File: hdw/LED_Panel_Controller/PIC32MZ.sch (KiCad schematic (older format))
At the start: 3 parts, among them U1101 PIC32MZ2048EFG100_IPF

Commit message: having a mid-project crisis
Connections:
- net WIFI_CHIP_EN: no longer names the net of U1101.79 (RD12/EBID12/ETXD2/RPD12/PMD12)
- net WIFI_Stream_Mode_LED renamed MLVDS_Stream_Mode_LED
- net WIFI_WAKE: no longer names the net of U1101.82 (RD5/~SQICS1~/RPD5)
- net ~WIFI_IRQN: no longer names the net of U1101.47 (RD14/AN32/AETXD0/RPD14)
- net ~WIFI_RESET: no longer names the net of U1101.81 (RD4/~SQICS0~/RPD4)
- net ~WIFI_SPI_SS: no longer names the net of U1101.80 (RD13/EBID13/ETXD3/PMD13)
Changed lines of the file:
@@
 Text GLabel 3020 5000 0    50   Input ~ 0
 PIC32MZ_SOSC_EC
-Text GLabel 7020 1700 2    40   Output ~ 0
-~WIFI_RESET
-Text GLabel 7020 1800 2    50   Output ~ 0
-WIFI_WAKE
-Text GLabel 7020 2200 2    50   Output ~ 0
-WIFI_CHIP_EN
 Text GLabel 7020 2000 2    50   Output ~ 0
 WIFI_SPI_SCK
-Text GLabel 7020 2300 2    40   Output ~ 0
-~WIFI_SPI_SS
 Text GLabel 7020 2100 2    50   Output ~ 0
 WIFI_SPI_MOSI
 Text GLabel 7020 2500 2    50   Input ~ 0
 WIFI_SPI_MISO
-Text GLabel 7020 2400 2    40   Input ~ 0
-~WIFI_IRQN
 $Comp
 L Custom_Library:GNDA_MZ #PWR01103
@@
 ~FLASH_SPI_CE7
 Text GLabel 3020 3450 0    50   Output ~ 0
-WIFI_Stream_Mode_LED
+MLVDS_Stream_Mode_LED
 Text Notes 9720 1950 0    50   ~ 0
 OC5

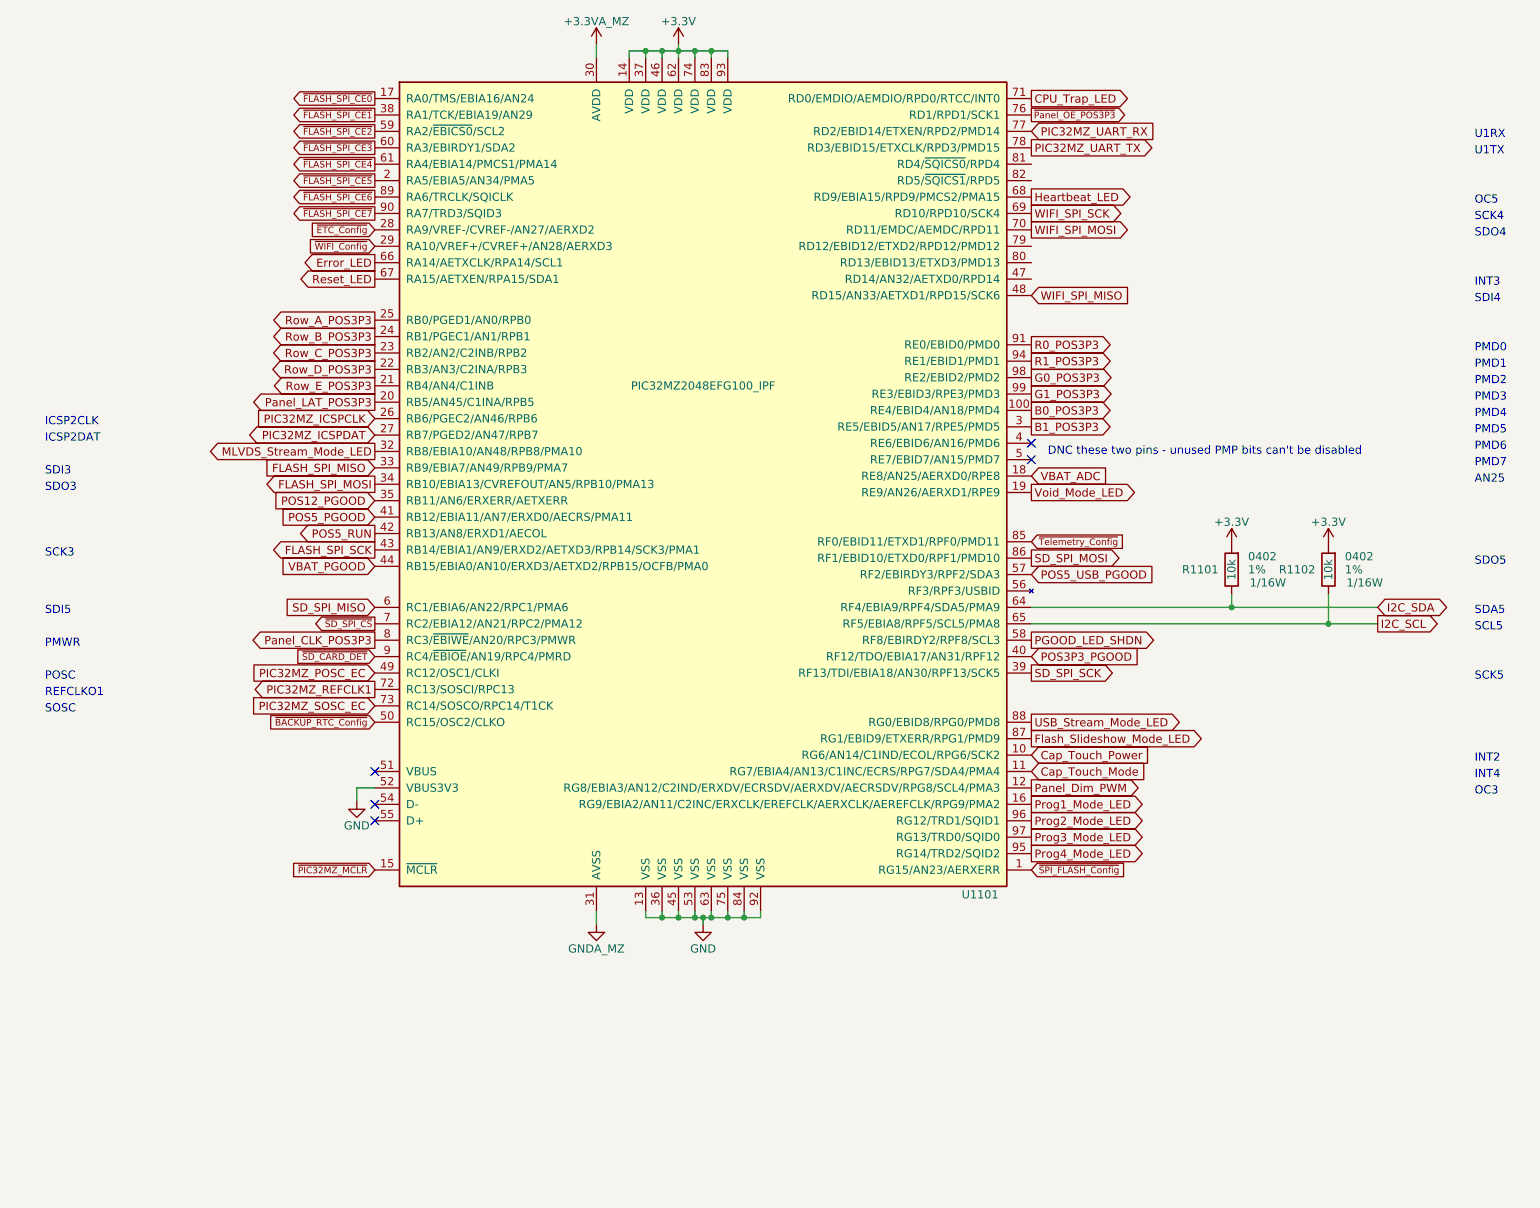
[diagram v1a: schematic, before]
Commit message: reworked schematic to use MLVDS connector instead of wifi module
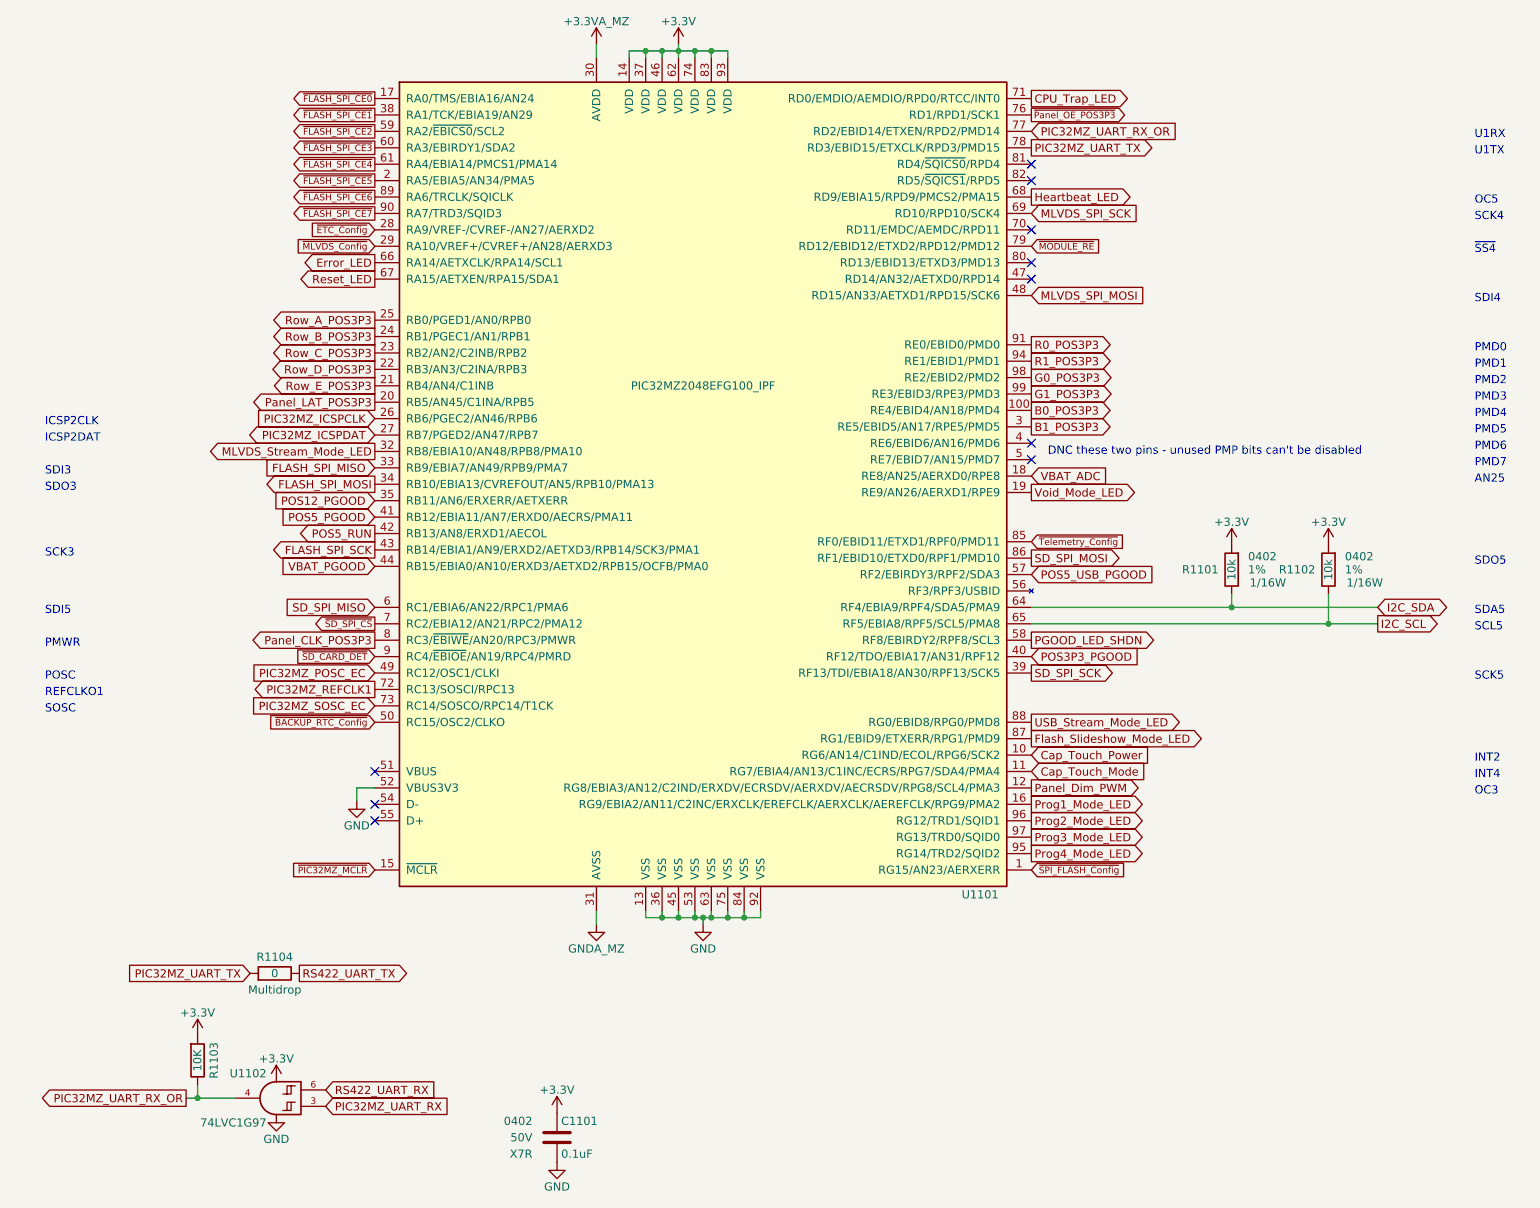
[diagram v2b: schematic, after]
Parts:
- added C1101: 0.1uF, Capacitors_SMD:C_0402, symbol Custom_Library:C_Custom
- added R1103: 10K, Resistors_SMD:R_0402, symbol Custom_Library:R_Custom
- added R1104: 0, Resistors_SMD:R_0402, symbol Custom_Library:R_Custom
- added U1102: 74LVC1G97, Package_TO_SOT_SMD:SOT-363_SC-70-6, symbol Custom_Library:74LVC1G97_Power_AND
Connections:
- net +3V3: now also C1101.1, R1103.1, U1102.5 (VCC)
- net GND: now also C1101.2, U1102.1 (GND), U1102.2 (GND)
- net PIC32MZ_UART_RX: now also U1102.3; no longer U1101.77 (RD2/EBID14/ETXEN/RPD2/PMD14)
- net PIC32MZ_UART_TX: now also R1104.1
- net ~MODULE_RE: now reaches U1101.79 (RD12/EBID12/ETXD2/RPD12/PMD12)
- net WIFI_SPI_MISO renamed MLVDS_SPI_MOSI
- net WIFI_SPI_MOSI: no longer names the net of U1101.70 (RD11/EMDC/AEMDC/RPD11)
- net WIFI_SPI_SCK renamed MLVDS_SPI_SCK
- net ~WIFI_Config renamed ~MLVDS_Config
- new net PIC32MZ_UART_RX_OR: R1103.2, U1101.77 (RD2/EBID14/ETXEN/RPD2/PMD14), U1102.4
- new net RS422_UART_RX: U1102.6
- new net RS422_UART_TX: R1104.2
- no-connect marks 5 -> 10
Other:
- note added: "~SS4"
- note removed: "INT3"
- note removed: "SDO4"
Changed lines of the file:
@@
 Sheet 11 34
 Title "LED Panel Controller"
-Date "2021-03-31"
+Date "2021-05-30"
 Rev "A"
 Comp "Drew Maatman"
@@
 PIC32MZ_UART_TX
 Text GLabel 7020 1500 2    50   Input ~ 0
-PIC32MZ_UART_RX
+PIC32MZ_UART_RX_OR
 Text GLabel 3020 3250 0    50   Input ~ 0
 PIC32MZ_ICSPCLK
@@
 Text GLabel 3020 5000 0    50   Input ~ 0
 PIC32MZ_SOSC_EC
-Text GLabel 7020 2000 2    50   Output ~ 0
-WIFI_SPI_SCK
-Text GLabel 7020 2100 2    50   Output ~ 0
-WIFI_SPI_MOSI
 Text GLabel 7020 2500 2    50   Input ~ 0
-WIFI_SPI_MISO
+MLVDS_SPI_MOSI
 $Comp
 L Custom_Library:GNDA_MZ #PWR01103
@@
 Text Notes 9720 2050 0    50   ~ 0
 SCK4
-Text Notes 9720 2150 0    50   ~ 0
-SDO4
-Text Notes 9720 2550 0    50   ~ 0
-SDI4
 Text Notes 9720 4850 0    50   ~ 0
 SCK5
@@
 Text GLabel 7020 5400 2    50   Input ~ 0
 Cap_Touch_Mode
-Text Notes 9720 2450 0    50   ~ 0
-INT3
 Text Notes 9720 5350 0    50   ~ 0
 INT2
@@
 Text GLabel 3020 2100 0    40   Input ~ 0
 ~ETC_Config
-Text GLabel 3020 2200 0    40   Input ~ 0
-~WIFI_Config
 Text GLabel 3020 5100 0    40   Input ~ 0
 ~BACKUP_RTC_Config
 Text GLabel 7020 6000 2    40   Input ~ 0
 ~SPI_FLASH_Config
+$Comp
+L Custom_Library:R_Custom R?
+U 1 1 60BFA971
+P 2410 6630
+AR Path="/5EAE2EF2/60BFA971" Ref="R?"  Part="1"
+AR Path="/5EAE30C7/60BFA971" Ref="R?"  Part="1"
+AR Path="/5EAE2D8A/60BFA971" Ref="R?"  Part="1"
+AR Path="/5EAE2D66/60BFA971" Ref="R?"  Part="1"
+AR Path="/5F581B41/60BFA971" Ref="R?"  Part="1"
+AR Path="/5F5829D3/60BFA971" Ref="R1104"  Part="1"
+F 0 "R1104" V 2310 6630 50  0000 C CNN
+F 1 "0" V 2410 6630 50  0000 C CNN
+F 2 "Resistors_SMD:R_0402" H 2410 6630 50  0001 C CNN
+F 3 "" H 2410 6630 50  0001 C CNN
+F 4 "0402" V 2510 6630 50  0001 C CNN "display_footprint"
+F 5 "1%" V 2610 6630 50  0001 C CNN "Tolerance"
+F 6 "1/16W" V 2710 6630 50  0001 C CNN "Wattage"
+F 7 "Multidrop" V 2510 6630 50  0000 C CNN "Configuration"
+F 8 "RMCF0402ZT0R00CT-ND" H 2410 6630 50  0001 C CNN "Digi-Key PN"
+	1    2410 6630
+	0    -1   1    0
+$EndComp
+Text GLabel 2260 6630 0    50   Input ~ 0
+PIC32MZ_UART_TX
+Text GLabel 2560 6630 2    50   Output ~ 0
+RS422_UART_TX
+$Comp
+L Custom_Library:74LVC1G97_Power_AND U1102
+U 1 1 60C055C7
+P 2420 7390
+F 0 "U1102" H 2480 7540 50  0000 L CNN
+F 1 "74LVC1G97" H 2480 7240 50  0000 L CNN
+F 2 "Package_TO_SOT_SMD:SOT-363_SC-70-6" H 2470 7390 50  0001 C CNN
+F 3 "http://www.ti.com/lit/ds/symlink/sn74lvc1g97.pdf" H 2470 7390 50  0001 C CNN
+	1    2420 7390
+	-1   0    0    -1
+$EndComp
+$Comp
+L power:GND #PWR0101
+U 1 1 60C05E46
+P 2420 7490
+F 0 "#PWR0101" H 2420 7240 50  0001 C CNN
+F 1 "GND" H 2420 7340 50  0000 C CNN
+F 2 "" H 2420 7490 50  0001 C CNN
+F 3 "" H 2420 7490 50  0001 C CNN
+	1    2420 7490
+	1    0    0    -1
+$EndComp
+$Comp
+L power:+3.3V #PWR0102
+U 1 1 60C060DB
+P 2420 7290
+F 0 "#PWR0102" H 2420 7140 50  0001 C CNN
+F 1 "+3.3V" H 2420 7430 50  0000 C CNN
+F 2 "" H 2420 7290 50  0001 C CNN
+F 3 "" H 2420 7290 50  0001 C CNN
+	1    2420 7290
+	1    0    0    -1
+$EndComp
+Text GLabel 1870 7390 0    50   Output ~ 0
+PIC32MZ_UART_RX_OR
+Text GLabel 2720 7440 2    50   Input ~ 0
+PIC32MZ_UART_RX
+Text GLabel 2720 7340 2    50   Input ~ 0
+RS422_UART_RX
+$Comp
+L Custom_Library:R_Custom R?
+U 1 1 60C11C11
+P 1940 7160
+AR Path="/5BAAE2B6/60C11C11" Ref="R?"  Part="1"
+AR Path="/5BB6CF6D/60C11C11" Ref="R?"  Part="1"
+AR Path="/5BBE424C/60C11C11" Ref="R?"  Part="1"
+AR Path="/5CB8A16A/60C11C11" Ref="R?"  Part="1"
+AR Path="/5F583BF6/60C11C11" Ref="R?"  Part="1"
+AR Path="/5F582E44/60C11C11" Ref="R?"  Part="1"
+AR Path="/5F5829D3/60C11C11" Ref="R1103"  Part="1"
+F 0 "R1103" V 1840 7160 50  0000 C CNN
+F 1 "10K" V 1940 7160 50  0000 C CNN
+F 2 "Resistors_SMD:R_0402" H 1940 7160 50  0001 C CNN
+F 3 "" H 1940 7160 50  0001 C CNN
+F 4 "0402" H 2010 7250 50  0001 L CNN "display_footprint"
+F 5 "1%" H 2010 7160 50  0001 L CNN "Tolerance"
+F 6 "1/16W" H 2010 7080 50  0001 L CNN "Wattage"
+F 7 "RMCF0402FT10K0CT-ND" H 2240 7560 60  0001 C CNN "Digi-Key PN"
+	1    1940 7160
+	-1   0    0    -1
+$EndComp
+$Comp
+L power:+3.3V #PWR0128
+U 1 1 60C1229E
+P 1940 7010
+F 0 "#PWR0128" H 1940 6860 50  0001 C CNN
+F 1 "+3.3V" H 1940 7150 50  0000 C CNN
+F 2 "" H 1940 7010 50  0001 C CNN
+F 3 "" H 1940 7010 50  0001 C CNN
+	1    1940 7010
+	1    0    0    -1
+$EndComp
+Wire Wire Line
+	2170 7390 1940 7390
+Wire Wire Line
+	1940 7310 1940 7390
+Connection ~ 1940 7390
+Wire Wire Line
+	1940 7390 1870 7390
+$Comp
+L power:GND #PWR?
+U 1 1 60C184F8
+P 4130 7780
+AR Path="/5F581B41/60C184F8" Ref="#PWR?"  Part="1"
+AR Path="/5F5829D3/60C184F8" Ref="#PWR0129"  Part="1"
+F 0 "#PWR0129" H 4130 7530 50  0001 C CNN
+F 1 "GND" H 4130 7630 50  0000 C CNN
+F 2 "" H 4130 7780 50  0001 C CNN
+F 3 "" H 4130 7780 50  0001 C CNN
+	1    4130 7780
+	1    0    0    -1
+$EndComp
+$Comp
+L Custom_Library:C_Custom C?
+U 1 1 60C18502
+P 4130 7630
+AR Path="/5BAAE16C/60C18502" Ref="C?"  Part="1"
+AR Path="/5BB181D8/60C18502" Ref="C?"  Part="1"
+AR Path="/5BB2595E/60C18502" Ref="C?"  Part="1"
+AR Path="/5BAAE0FA/60C18502" Ref="C?"  Part="1"
+AR Path="/5BB86F23/60C18502" Ref="C?"  Part="1"
+AR Path="/5D77A516/60C18502" Ref="C?"  Part="1"
+AR Path="/5E939CFF/60C18502" Ref="C?"  Part="1"
+AR Path="/5EAE2D66/60C18502" Ref="C?"  Part="1"
+AR Path="/5F581B41/60C18502" Ref="C?"  Part="1"
+AR Path="/5F5829D3/60C18502" Ref="C1101"  Part="1"
+F 0 "C1101" H 4155 7730 50  0000 L CNN
+F 1 "0.1uF" H 4155 7530 50  0000 L CNN
+F 2 "Capacitors_SMD:C_0402" H 4168 7480 50  0001 C CNN
+F 3 "" H 4155 7730 50  0001 C CNN
+F 4 "0402" H 3980 7730 50  0000 R CNN "display_footprint"
+F 5 "50V" H 3980 7630 50  0000 R CNN "Voltage"
+F 6 "X7R" H 3980 7530 50  0000 R CNN "Dielectric"
+F 7 "490-10701-1-ND" H 4555 8130 60  0001 C CNN "Digi-Key PN"
+	1    4130 7630
+	1    0    0    -1
+$EndComp
+$Comp
+L power:+3.3V #PWR0130
+U 1 1 60C18D05
+P 4130 7480
+F 0 "#PWR0130" H 4130 7330 50  0001 C CNN
+F 1 "+3.3V" H 4130 7620 50  0000 C CNN
+F 2 "" H 4130 7480 50  0001 C CNN
+F 3 "" H 4130 7480 50  0001 C CNN
+	1    4130 7480
+	1    0    0    -1
+$EndComp
+Text GLabel 7020 2200 2    40   Input ~ 0
+~MODULE_RE
+Text Notes 9720 2250 0    50   ~ 0
+~SS4
+Text GLabel 7020 2000 2    50   Input ~ 0
+MLVDS_SPI_SCK
+NoConn ~ 7020 1700
+NoConn ~ 7020 1800
+NoConn ~ 7020 2100
+NoConn ~ 7020 2300
+NoConn ~ 7020 2400
+Text Notes 9720 2550 0    50   ~ 0
+SDI4
+Text GLabel 3020 2200 0    40   Input ~ 0
+~MLVDS_Config
 $EndSCHEMATC

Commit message: added some more digikey part numbers to schematic
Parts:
- U1102: Digi-Key PN (none) -> 1727-1772-1-ND
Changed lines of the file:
@@
 F 2 "Package_TO_SOT_SMD:SOT-363_SC-70-6" H 2470 7390 50  0001 C CNN
 F 3 "http://www.ti.com/lit/ds/symlink/sn74lvc1g97.pdf" H 2470 7390 50  0001 C CNN
+F 4 "1727-1772-1-ND" H 2420 7390 50  0001 C CNN "Digi-Key PN"
 	1    2420 7390
 	-1   0    0    -1

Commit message: added BOMs, some consolidation
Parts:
- C1101: Digi-Key PN 490-10701-1-ND -> 490-10698-1-ND
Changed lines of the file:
@@
 F 5 "50V" H 3980 7630 50  0000 R CNN "Voltage"
 F 6 "X7R" H 3980 7530 50  0000 R CNN "Dielectric"
-F 7 "490-10701-1-ND" H 4555 8130 60  0001 C CNN "Digi-Key PN"
+F 7 "490-10698-1-ND" H 4555 8130 60  0001 C CNN "Digi-Key PN"
 	1    4130 7630
 	1    0    0    -1
